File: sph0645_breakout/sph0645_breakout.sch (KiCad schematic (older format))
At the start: 3 parts, among them J1 GS3, J2 CONN_01X06, U1 SPH0645LM4H-B

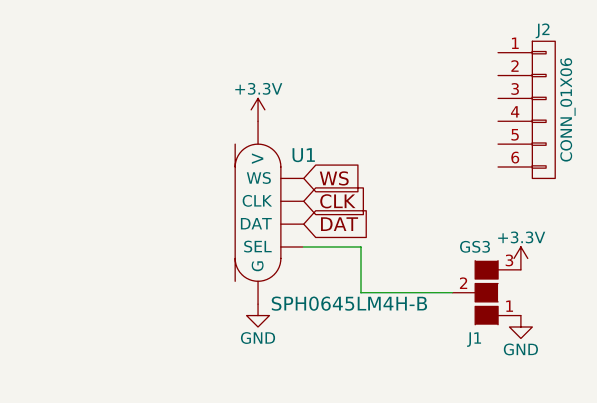
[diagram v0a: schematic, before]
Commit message: Finished I2S microphone mod board
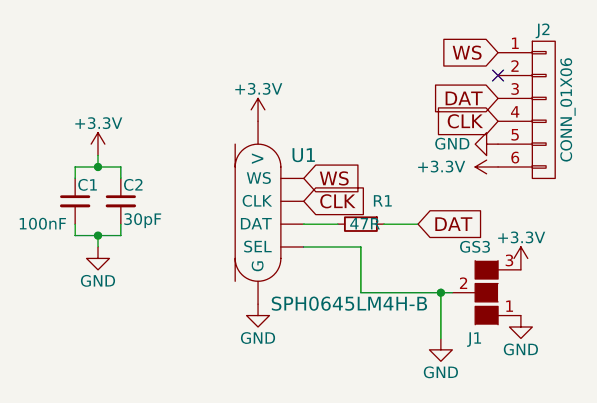
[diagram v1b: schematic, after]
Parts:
- added C1: 100nF, Capacitors_SMD:C_0603, symbol C_Small
- added C2: 30pF, Capacitors_SMD:C_0603, symbol C_Small
- added R1: 47R, Resistors_SMD:R_0603_HandSoldering, symbol R_Small
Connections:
- net +3V3: now also J2.6 (P6), C1.1, C2.1
- net CLK: now also J2.4 (P4)
- net DAT: now also J2.3 (P3), R1.1; no longer U1.6 (DAT)
- net GND: now also J1.2 (G2), J2.5 (P5), U1.2 (SEL), C1.2, C2.2
- net WS: now also J2.1 (P1)
- new net: R1.2, U1.6 (DAT)
- no-connect marks 0 -> 1
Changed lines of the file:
@@
 LIBS:valves
 LIBS:sph0645
+LIBS:sph0645_breakout-cache
 EELAYER 25 0
 EELAYER END
@@
 Text GLabel 5500 3200 2    60   Input ~ 0
 CLK
-Text GLabel 5500 3300 2    60   Input ~ 0
+Text GLabel 6000 3300 2    60   Input ~ 0
 DAT
 $Comp
@@
 	1    0    0    -1
 $EndComp
+$Comp
+L +3.3V #PWR05
+U 1 1 59AEA01B
+P 6350 3050
+F 0 "#PWR05" H 6350 2900 50  0001 C CNN
+F 1 "+3.3V" V 6350 3300 50  0000 C CNN
+F 2 "" H 6350 3050 50  0001 C CNN
+F 3 "" H 6350 3050 50  0001 C CNN
+	1    6350 3050
+	0    -1   -1   0
+$EndComp
+$Comp
+L GND #PWR06
+U 1 1 59AEA042
+P 6350 2950
+F 0 "#PWR06" H 6350 2700 50  0001 C CNN
+F 1 "GND" V 6350 2750 50  0000 C CNN
+F 2 "" H 6350 2950 50  0001 C CNN
+F 3 "" H 6350 2950 50  0001 C CNN
+	1    6350 2950
+	0    1    1    0
+$EndComp
+Text GLabel 6350 2850 0    60   Input ~ 0
+CLK
+Text GLabel 6350 2750 0    60   Input ~ 0
+DAT
+Text GLabel 6350 2550 0    60   Input ~ 0
+WS
+NoConn ~ 6350 2650
+$Comp
+L GND #PWR07
+U 1 1 59AEB063
+P 6100 3800
+F 0 "#PWR07" H 6100 3550 50  0001 C CNN
+F 1 "GND" H 6100 3650 50  0000 C CNN
+F 2 "" H 6100 3800 50  0001 C CNN
+F 3 "" H 6100 3800 50  0001 C CNN
+	1    6100 3800
+	1    0    0    -1
+$EndComp
+Wire Wire Line
+	6100 3800 6100 3600
+Connection ~ 6100 3600
+$Comp
+L C_Small C1
+U 1 1 59ADED61
+P 4500 3200
+F 0 "C1" H 4510 3270 50  0000 L CNN
+F 1 "100nF" H 4250 3100 50  0000 L CNN
+F 2 "Capacitors_SMD:C_0603" H 4500 3200 50  0001 C CNN
+F 3 "" H 4500 3200 50  0001 C CNN
+	1    4500 3200
+	1    0    0    -1
+$EndComp
+$Comp
+L C_Small C2
+U 1 1 59ADEDA8
+P 4700 3200
+F 0 "C2" H 4710 3270 50  0000 L CNN
+F 1 "30pF" H 4710 3120 50  0000 L CNN
+F 2 "Capacitors_SMD:C_0603" H 4700 3200 50  0001 C CNN
+F 3 "" H 4700 3200 50  0001 C CNN
+	1    4700 3200
+	1    0    0    -1
+$EndComp
+$Comp
+L +3.3V #PWR08
+U 1 1 59ADEE4B
+P 4600 3000
+F 0 "#PWR08" H 4600 2850 50  0001 C CNN
+F 1 "+3.3V" H 4600 3140 50  0000 C CNN
+F 2 "" H 4600 3000 50  0001 C CNN
+F 3 "" H 4600 3000 50  0001 C CNN
+	1    4600 3000
+	1    0    0    -1
+$EndComp
+$Comp
+L GND #PWR09
+U 1 1 59ADEE80
+P 4600 3400
+F 0 "#PWR09" H 4600 3150 50  0001 C CNN
+F 1 "GND" H 4600 3250 50  0000 C CNN
+F 2 "" H 4600 3400 50  0001 C CNN
+F 3 "" H 4600 3400 50  0001 C CNN
+	1    4600 3400
+	1    0    0    -1
+$EndComp
+Wire Wire Line
+	4500 3100 4500 3050
+Wire Wire Line
+	4500 3050 4700 3050
+Wire Wire Line
+	4700 3050 4700 3100
+Wire Wire Line
+	4600 3000 4600 3050
+Connection ~ 4600 3050
+Wire Wire Line
+	4500 3300 4500 3350
+Wire Wire Line
+	4500 3350 4700 3350
+Wire Wire Line
+	4700 3350 4700 3300
+Wire Wire Line
+	4600 3400 4600 3350
+Connection ~ 4600 3350
+$Comp
+L R_Small R1
+U 1 1 59ADF17D
+P 5750 3300
+F 0 "R1" V 5650 3350 50  0000 L CNN
+F 1 "47R" V 5750 3250 50  0000 L CNN
+F 2 "Resistors_SMD:R_0603_HandSoldering" H 5750 3300 50  0001 C CNN
+F 3 "" H 5750 3300 50  0001 C CNN
+	1    5750 3300
+	0    1    1    0
+$EndComp
+Wire Wire Line
+	5850 3300 6000 3300
+Wire Wire Line
+	5650 3300 5500 3300
 $EndSCHEMATC
